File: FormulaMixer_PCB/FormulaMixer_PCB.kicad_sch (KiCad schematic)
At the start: 16 parts

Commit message: Add unsaved progress
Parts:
- added R?: 10k, Resistor_SMD:R_0603_1608Metric, symbol Device:R_Small_US
- added SW?: SW_Push, Button_Switch_SMD:SW_SPST_EVPBF, symbol Switch:SW_Push
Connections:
- net +3V3: now also R?.1
- net GND: now also SW?.1
- net BTN: now reaches ESP32-WROOM-32D?.9 (IO33)
- net BTN: now also R?.2, SW?.2
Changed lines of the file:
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@@
   (junction (at 253.492 93.472) (diameter 0) (color 0 0 0 0)
   )
+  (junction (at 65.532 31.75) (diameter 0) (color 0 0 0 0)
+  )
   (junction (at 271.653 110.744) (diameter 0) (color 0 0 0 0)
   )
@@
     (stroke (width 0) (type default) (color 0 0 0 0))
   )
+  (wire (pts (xy 152.654 88.392) (xy 160.02 88.392))
+    (stroke (width 0) (type default) (color 0 0 0 0))
+  )
   (wire (pts (xy 137.414 101.092) (xy 137.414 102.362))
     (stroke (width 0) (type default) (color 0 0 0 0))
@@
     (stroke (width 0) (type default) (color 0 0 0 0))
   )
+  (wire (pts (xy 65.532 31.75) (xy 65.532 33.782))
+    (stroke (width 0) (type default) (color 0 0 0 0))
+  )
   (wire (pts (xy 44.958 155.702) (xy 49.784 155.702))
     (stroke (width 0) (type default) (color 0 0 0 0))
@@
     (stroke (width 0) (type default) (color 0 0 0 0))
   )
+  (wire (pts (xy 65.532 30.226) (xy 65.532 31.75))
+    (stroke (width 0) (type default) (color 0 0 0 0))
+  )
   (wire (pts (xy 203.962 45.72) (xy 207.772 45.72))
     (stroke (width 0) (type default) (color 0 0 0 0))
@@
     (stroke (width 0) (type default) (color 0 0 0 0))
   )
+  (wire (pts (xy 65.532 21.336) (xy 65.532 25.146))
+    (stroke (width 0) (type default) (color 0 0 0 0))
+  )
   (wire (pts (xy 152.654 93.472) (xy 160.02 93.472))
     (stroke (width 0) (type default) (color 0 0 0 0))
@@
     (stroke (width 0) (type default) (color 0 0 0 0))
   )
+  (wire (pts (xy 65.532 31.75) (xy 75.184 31.75))
+    (stroke (width 0) (type default) (color 0 0 0 0))
+  )
   (wire (pts (xy 272.034 56.642) (xy 272.034 61.722))
     (stroke (width 0) (type default) (color 0 0 0 0))
@@
     (effects (font (size 1.27 1.27)) (justify left bottom))
   )
+  (label "BTN" (at 75.184 31.75 0)
+    (effects (font (size 1.27 1.27)) (justify left bottom))
+  )
   (label "DTR" (at 272.034 38.862 0)
     (effects (font (size 1.27 1.27)) (justify left bottom))
@@
   )
   (label "DB6" (at 167.64 60.452 0)
+    (effects (font (size 1.27 1.27)) (justify left bottom))
+  )
+  (label "BTN" (at 160.02 88.392 0)
     (effects (font (size 1.27 1.27)) (justify left bottom))
   )
@@
     (pin "1")
   )
+  (symbol (lib_id "power:+3.3V") (at 65.532 21.336 0) (unit 1)
+    (in_bom yes) (on_board yes) (fields_autoplaced)
+    (property "Reference" "#PWR?" (id 0) (at 65.532 25.146 0)
+      (effects (font (size 1.27 1.27)) hide)
+    )
+    (property "Value" "+3.3V" (id 1) (at 65.532 16.256 0))
+    (property "Footprint" "" (id 2) (at 65.532 21.336 0)
+      (effects (font (size 1.27 1.27)) hide)
+    )
+    (property "Datasheet" "" (id 3) (at 65.532 21.336 0)
+      (effects (font (size 1.27 1.27)) hide)
+    )
+    (pin "1")
+  )
   (symbol (lib_id "Device:C") (at 274.193 114.554 0) (unit 1)
     (in_bom yes) (on_board yes) (fields_autoplaced)
@@
     )
     (pin "1")
+  )
+  (symbol (lib_id "power:GND") (at 65.532 43.942 0) (unit 1)
+    (in_bom yes) (on_board yes) (fields_autoplaced)
+    (property "Reference" "#PWR?" (id 0) (at 65.532 50.292 0)
+      (effects (font (size 1.27 1.27)) hide)
+    )
+    (property "Value" "GND" (id 1) (at 65.532 49.022 0))
+    (property "Footprint" "" (id 2) (at 65.532 43.942 0)
+      (effects (font (size 1.27 1.27)) hide)
+    )
+    (property "Datasheet" "" (id 3) (at 65.532 43.942 0)
+      (effects (font (size 1.27 1.27)) hide)
+    )
+    (pin "1")
+  )
+  (symbol (lib_id "Switch:SW_Push") (at 65.532 38.862 90) (unit 1)
+    (in_bom yes) (on_board yes) (fields_autoplaced)
+    (property "Reference" "SW?" (id 0) (at 66.802 37.5919 90)
+      (effects (font (size 1.27 1.27)) (justify right))
+    )
+    (property "Value" "SW_Push" (id 1) (at 66.802 40.1319 90)
+      (effects (font (size 1.27 1.27)) (justify right))
+    )
+    (property "Footprint" "Button_Switch_SMD:SW_SPST_EVPBF" (id 2) (at 60.452 38.862 0)
+      (effects (font (size 1.27 1.27)) hide)
+    )
+    (property "Datasheet" "~" (id 3) (at 60.452 38.862 0)
+      (effects (font (size 1.27 1.27)) hide)
+    )
+    (pin "1")
+    (pin "2")
   )
   (symbol (lib_id "power:GND") (at 250.063 115.824 0) (unit 1)
@@
     )
     (property "Datasheet" "~" (id 3) (at 258.064 27.432 0)
+      (effects (font (size 1.27 1.27)) hide)
+    )
+    (pin "1")
+    (pin "2")
+  )
+  (symbol (lib_id "Device:R_Small_US") (at 65.532 27.686 0) (unit 1)
+    (in_bom yes) (on_board yes) (fields_autoplaced)
+    (property "Reference" "R?" (id 0) (at 68.072 26.4159 0)
+      (effects (font (size 1.27 1.27)) (justify left))
+    )
+    (property "Value" "10k" (id 1) (at 68.072 28.9559 0)
+      (effects (font (size 1.27 1.27)) (justify left))
+    )
+    (property "Footprint" "Resistor_SMD:R_0603_1608Metric" (id 2) (at 65.532 27.686 0)
+      (effects (font (size 1.27 1.27)) hide)
+    )
+    (property "Datasheet" "~" (id 3) (at 65.532 27.686 0)
       (effects (font (size 1.27 1.27)) hide)
     )
@@
       (reference "#PWR?") (unit 1) (value "+5V") (footprint "")
     )
+    (path "/98c267d0-712b-4076-993e-1b9dcaf303bc"
+      (reference "#PWR?") (unit 1) (value "+3.3V") (footprint "")
+    )
     (path "/9af09445-6d28-4d33-a007-92659018b91b"
       (reference "#PWR?") (unit 1) (value "+3.3V") (footprint "")
     )
+    (path "/9ba1e01e-4995-4bd2-b509-98b8075a98ac"
+      (reference "#PWR?") (unit 1) (value "GND") (footprint "")
+    )
     (path "/bf552638-299c-49a7-b642-2353ac57797b"
       (reference "#PWR?") (unit 1) (value "GND") (footprint "")
@@
       (reference "R?") (unit 1) (value "10k") (footprint "Resistor_SMD:R_0603_1608Metric")
     )
+    (path "/d185bb2b-82b8-4844-90f8-e546fe5c950d"
+      (reference "R?") (unit 1) (value "10k") (footprint "Resistor_SMD:R_0603_1608Metric")
+    )
     (path "/f92f691d-1877-4e2c-aff7-89d6c686d00f"
       (reference "R?") (unit 1) (value "10k") (footprint "Resistor_SMD:R_0603_1608Metric")
@@
       (reference "SW?") (unit 1) (value "RotaryEncoder_Switch") (footprint "")
     )
+    (path "/b6158e9f-46a0-4727-bb51-a27a65b8db5f"
+      (reference "SW?") (unit 1) (value "SW_Push") (footprint "Button_Switch_SMD:SW_SPST_EVPBF")
+    )
     (path "/1e5f7901-dd03-4533-a2fb-24b6a8c35075"

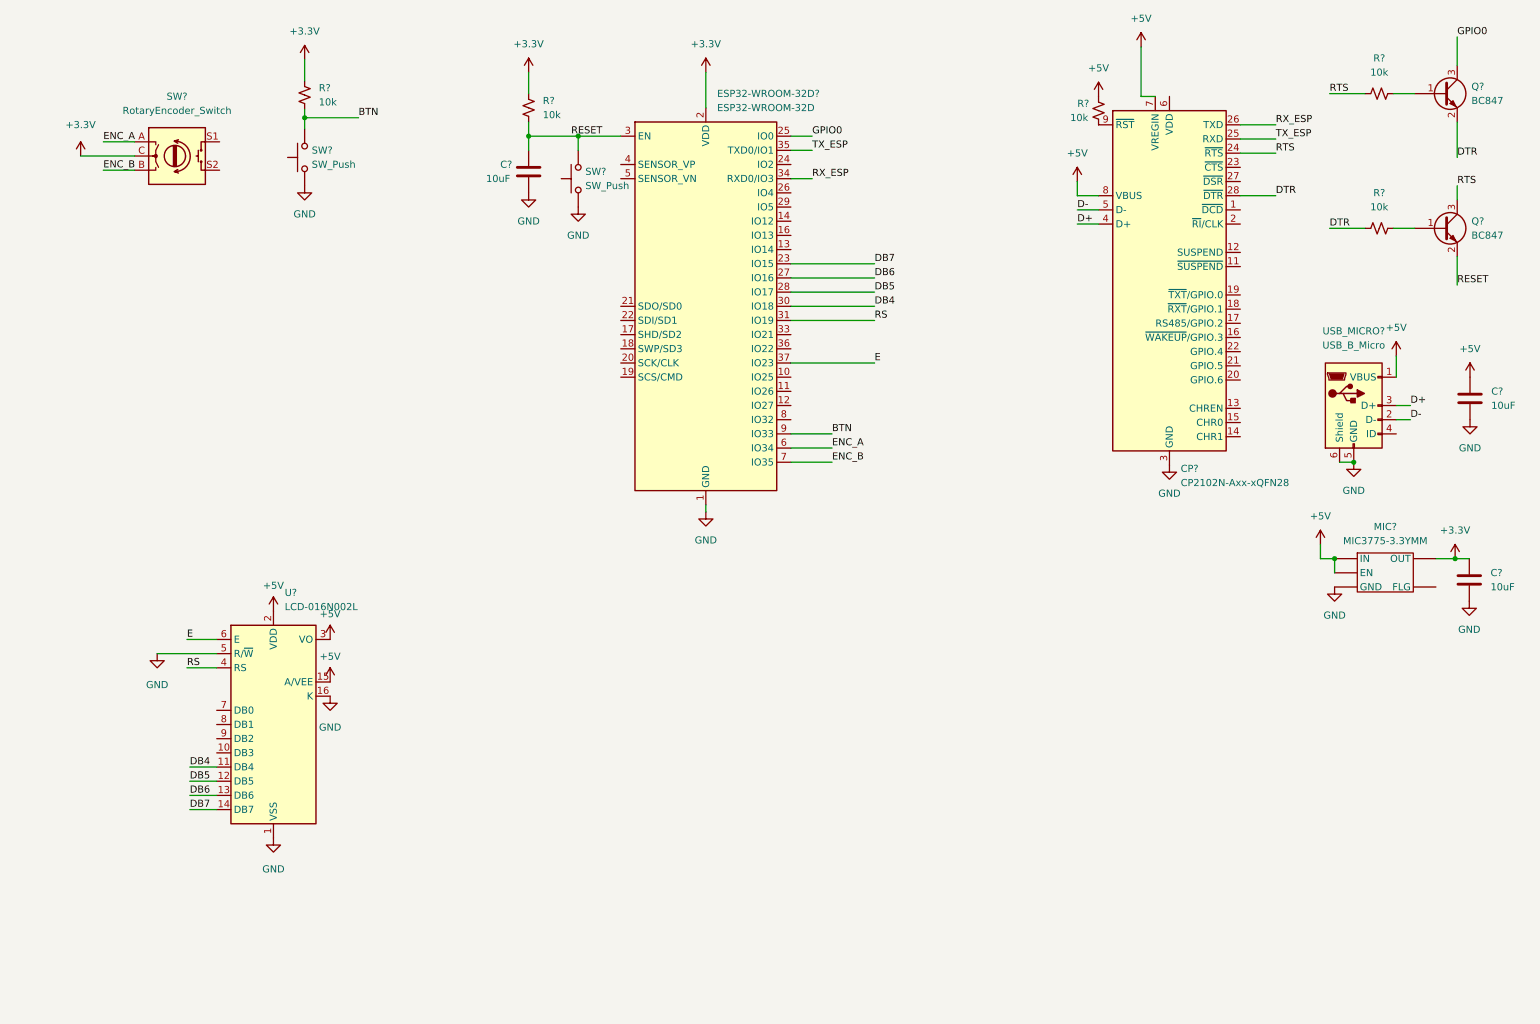
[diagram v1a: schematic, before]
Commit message: Add Demuxes and H-Bridges to schematic
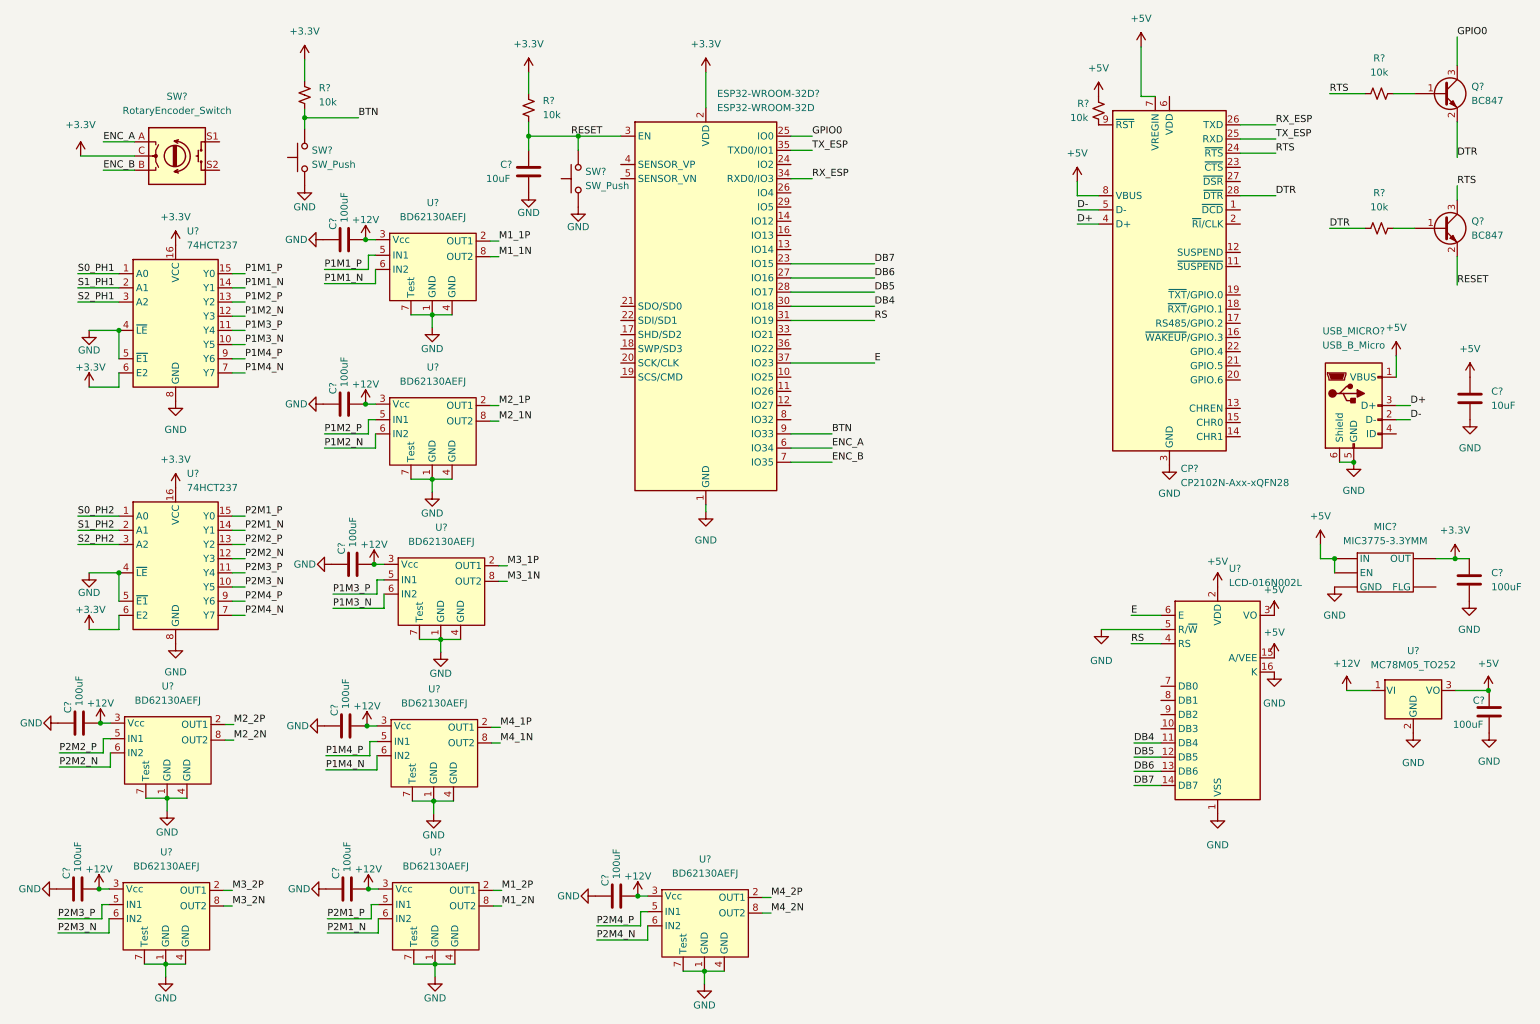
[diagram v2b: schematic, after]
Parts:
- added C? (x9): 100uF, Capacitor_SMD:C_0603_1608Metric, symbol Device:C
- added U? (x2): 74HCT237, symbol 74xx:74HCT237
- added U? (x8): BD62130AEFJ, symbol WyattLib:BD62130AEFJ
- added U?: MC78M05_TO252, Package_TO_SOT_SMD:TO-252-2, symbol Regulator_Linear:MC78M05_TO252
- C?: value 10uF -> 100uF
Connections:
- net +3V3: now also U?.16 (VCC), U?.16 (VCC), U?.6 (E2), U?.6 (E2)
- net +5V: now also C?.1, U?.3 (VO)
- net GND: now also C?.1, C?.1, C?.1, C?.1, C?.1, C?.1, C?.1, C?.1, C?.2, U?.1 (GND), U?.1 (GND), U?.1 (GND), U?.1 (GND), U?.1 (GND), U?.1 (GND), U?.1 (GND), U?.1 (GND), U?.2 (GND), U?.4 (GND), U?.4 (GND), U?.4 (GND), U?.4 (GND), U?.4 (GND), U?.4 (GND), U?.4 (GND), U?.4 (GND), U?.4 (~{LE}), U?.4 (~{LE}), U?.5 (~{E1}), U?.5 (~{E1}), U?.7 (Test), U?.7 (Test), U?.7 (Test), U?.7 (Test), U?.7 (Test), U?.7 (Test), U?.7 (Test), U?.7 (Test), U?.8 (GND), U?.8 (GND)
- new net +12V: C?.2, C?.2, C?.2, C?.2, C?.2, C?.2, C?.2, C?.2, U?.1 (VI), U?.3 (Vcc), U?.3 (Vcc), U?.3 (Vcc), U?.3 (Vcc), U?.3 (Vcc), U?.3 (Vcc), U?.3 (Vcc), U?.3 (Vcc)
- new net M1_1N: U?.8 (OUT2)
- new net M1_1P: U?.2 (OUT1)
- new net M1_2N: U?.8 (OUT2)
- new net M1_2P: U?.2 (OUT1)
- new net M2_1N: U?.8 (OUT2)
- new net M2_1P: U?.2 (OUT1)
- new net M2_2N: U?.8 (OUT2)
- new net M2_2P: U?.2 (OUT1)
- new net M3_1N: U?.8 (OUT2)
- new net M3_1P: U?.2 (OUT1)
- new net M3_2N: U?.8 (OUT2)
- new net M3_2P: U?.2 (OUT1)
- new net M4_1N: U?.8 (OUT2)
- new net M4_1P: U?.2 (OUT1)
- new net M4_2N: U?.8 (OUT2)
- new net M4_2P: U?.2 (OUT1)
- new net P1M1_N: U?.14 (Y1), U?.6 (IN2)
- new net P1M1_P: U?.15 (Y0), U?.5 (IN1)
- new net P1M2_N: U?.12 (Y3), U?.6 (IN2)
- new net P1M2_P: U?.13 (Y2), U?.5 (IN1)
- new net P1M3_N: U?.10 (Y5), U?.6 (IN2)
- new net P1M3_P: U?.11 (Y4), U?.5 (IN1)
- new net P1M4_N: U?.6 (IN2), U?.7 (Y7)
- new net P1M4_P: U?.5 (IN1), U?.9 (Y6)
- new net P2M1_N: U?.14 (Y1), U?.6 (IN2)
- new net P2M1_P: U?.15 (Y0), U?.5 (IN1)
- new net P2M2_N: U?.12 (Y3), U?.6 (IN2)
- new net P2M2_P: U?.13 (Y2), U?.5 (IN1)
- new net P2M3_N: U?.10 (Y5), U?.6 (IN2)
- new net P2M3_P: U?.11 (Y4), U?.5 (IN1)
- new net P2M4_N: U?.6 (IN2), U?.7 (Y7)
- new net P2M4_P: U?.5 (IN1), U?.9 (Y6)
- new net S0_PH1: U?.1 (A0)
- new net S0_PH2: U?.1 (A0)
- new net S1_PH1: U?.2 (A1)
- new net S1_PH2: U?.2 (A1)
- new net S2_PH1: U?.3 (A2)
- new net S2_PH2: U?.3 (A2)
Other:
- moved on the sheet: U?

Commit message: Add connectors to schematic
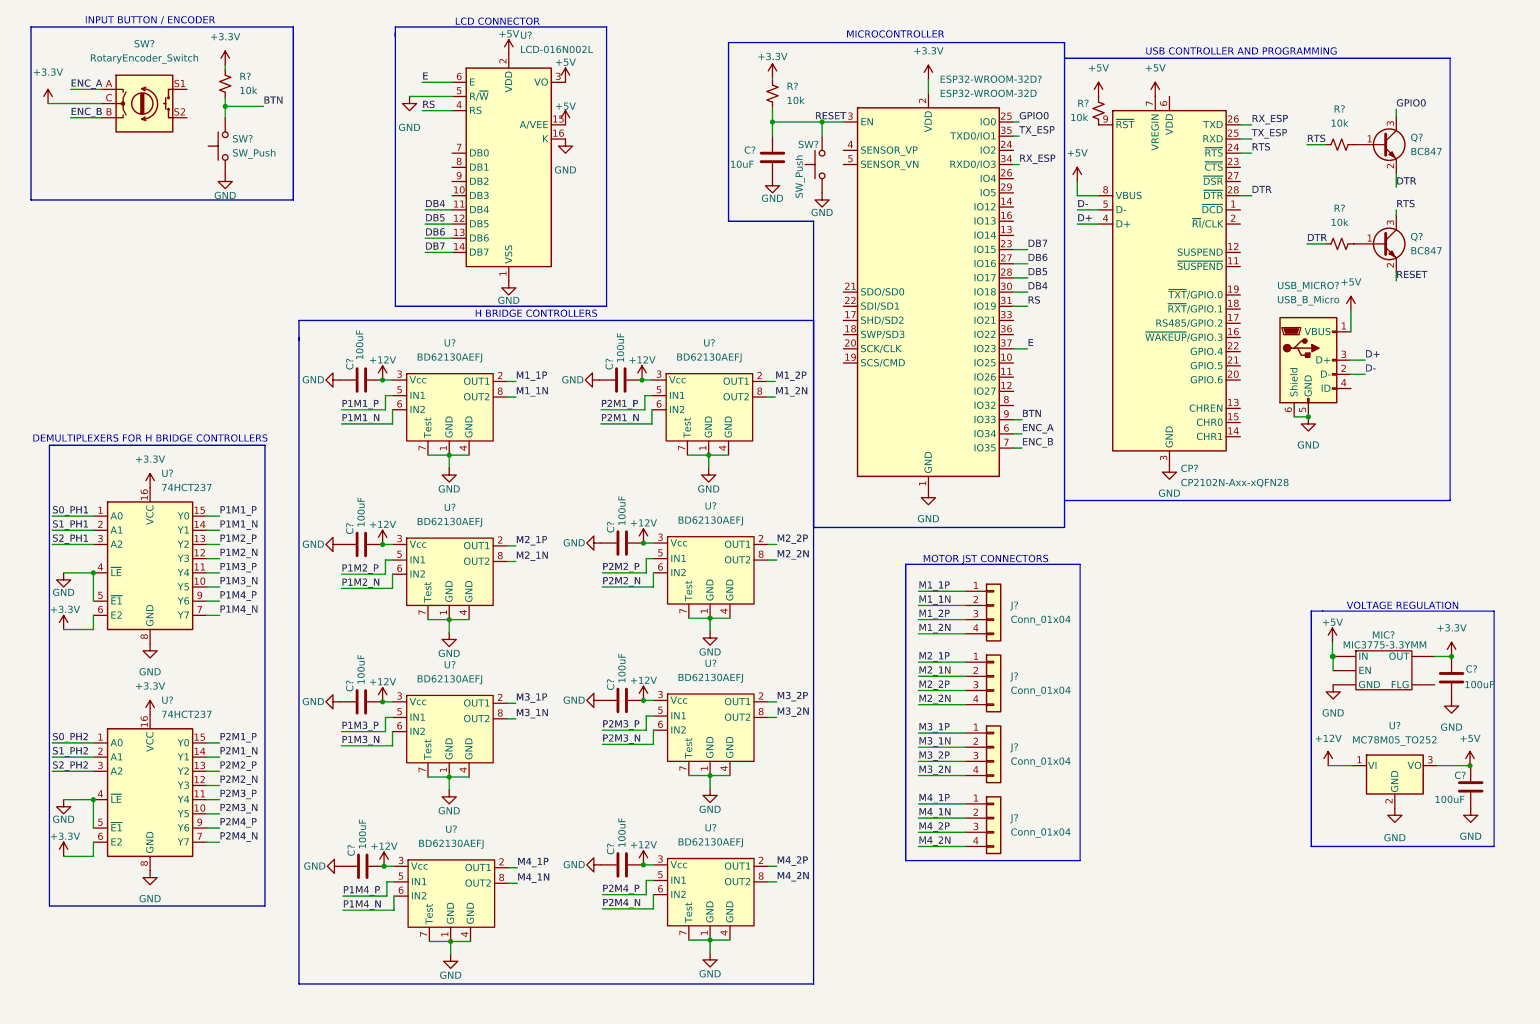
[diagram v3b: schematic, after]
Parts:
- removed C?: 10uF, Capacitor_SMD:C_0603_1608Metric, symbol Device:C
- added J? (x4): Conn_01x04, symbol Connector_Generic:Conn_01x04
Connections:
- net M1_1N: now also J?.2 (Pin_2)
- net M1_1P: now also J?.1 (Pin_1)
- net M1_2N: now also J?.4 (Pin_4)
- net M1_2P: now also J?.3 (Pin_3)
- net M2_1N: now also J?.2 (Pin_2)
- net M2_1P: now also J?.1 (Pin_1)
- net M2_2N: now also J?.4 (Pin_4)
- net M2_2P: now also J?.3 (Pin_3)
- net M3_1N: now also J?.2 (Pin_2)
- net M3_1P: now also J?.1 (Pin_1)
- net M3_2N: now also J?.4 (Pin_4)
- net M3_2P: now also J?.3 (Pin_3)
- net M4_1N: now also J?.2 (Pin_2)
- net M4_1P: now also J?.1 (Pin_1)
- net M4_2N: now also J?.4 (Pin_4)
- net M4_2P: now also J?.3 (Pin_3)
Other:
- note added: "DEMULTIPLEXERS FOR H BRIDGE CONTROLLERS"
- note added: "H BRIDGE CONTROLLERS"
- note added: "INPUT BUTTON / ENCODER"
- note added: "LCD CONNECTOR"
- note added: "MICROCONTROLLER"
- note added: "MOTOR JST CONNECTORS"
- note added: "USB CONTROLLER AND PROGRAMMING"
- note added: "VOLTAGE REGULATION"
- moved on the sheet: C?, ESP32-WROOM-32D?, MIC?, Q?, R?, SW?, U?, USB_MICRO?

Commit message: Finish Schematic
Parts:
- removed SW?: SW_Push, Button_Switch_SMD:SW_SPST_EVPBF, symbol Switch:SW_Push
- added J5: Conn_01x02, symbol Connector_Generic:Conn_01x02
- added R2: 10k, Resistor_SMD:R_0603_1608Metric, symbol Device:R_Small_US
- added SW2: SW_Push, Button_Switch_SMD:SW_SPST_EVPBF, symbol Switch:SW_Push
- gave numbers to parts that had none: 40
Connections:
- net S0_PH1 is gone; now on net S0_P1: U1.1 (A0)
- net S0_PH2 is gone; now on net S0_P2: U2.1 (A0)
- net S1_PH1 is gone; now on net S1_P1: U1.2 (A1)
- net S1_PH2 is gone; now on net S1_P2: U2.2 (A1)
- net S2_PH1 is gone; now on net S2_P1: U1.3 (A2)
- net S2_PH2 is gone; now on net S2_P2: U2.3 (A2)
- net +12V: now also J5.1 (Pin_1)
- net +3V3: now also R2.1
- net BTN: now also R2.2, SW2.2; no longer R1.2
- net DB7: now also ESP32-WROOM-32D1.16 (IO13); no longer ESP32-WROOM-32D1.23 (IO15)
- net GND: now also SW1.S2, J5.2 (Pin_2), SW2.1
- net ENC_BTN: now reaches SW1.S1
- net ENC_BTN: now also ESP32-WROOM-32D1.8 (IO32), R1.2
- net S0_P1: now reaches ESP32-WROOM-32D1.10 (IO25)
- net S1_P1: now reaches ESP32-WROOM-32D1.11 (IO26)
- net S2_P1: now reaches ESP32-WROOM-32D1.12 (IO27)
- net S2_P2: now reaches ESP32-WROOM-32D1.13 (IO14)
- net S0_P2: now reaches ESP32-WROOM-32D1.33 (IO21)
- net S1_P2: now reaches ESP32-WROOM-32D1.36 (IO22)
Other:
- note added: "POWER INPUT"
- moved on the sheet: R1

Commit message: Assign all footprints
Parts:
- J1, J2, J3, J4: footprint (none) -> Connector_JST:JST_XH_B4B-XH-A_1x04_P2.50mm_Vertical
- J5: footprint (none) -> Connector_JST:JST_XH_B2B-XH-A_1x02_P2.50mm_Vertical
- SW1: footprint (none) -> Connector_JST_Downloaded:PEC12R-4xxF-Sxxxx
- U1, U2: footprint (none) -> Package_SO:SOIC-16_3.9x9.9mm_P1.27mm
- U10, U11, U3, U4, U5, U6, U8, U9: footprint (none) -> Package_SO:SOIC-8-1EP_3.9x4.9mm_P1.27mm_EP2.514x3.2mm_ThermalVias
- U7: footprint Display:LCD-016N002L -> Connector_JST_Downloaded:LCD_HEADER
